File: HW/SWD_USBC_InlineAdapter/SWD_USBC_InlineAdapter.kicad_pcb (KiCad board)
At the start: 4 copper layers, 15.2 x 17.8 mm, 7 parts, among them J1 Conn_ARM_JTAG_SWD_10, J5 USB_C_Receptacle_USB2.0_14P, P1 USB_C_Plug

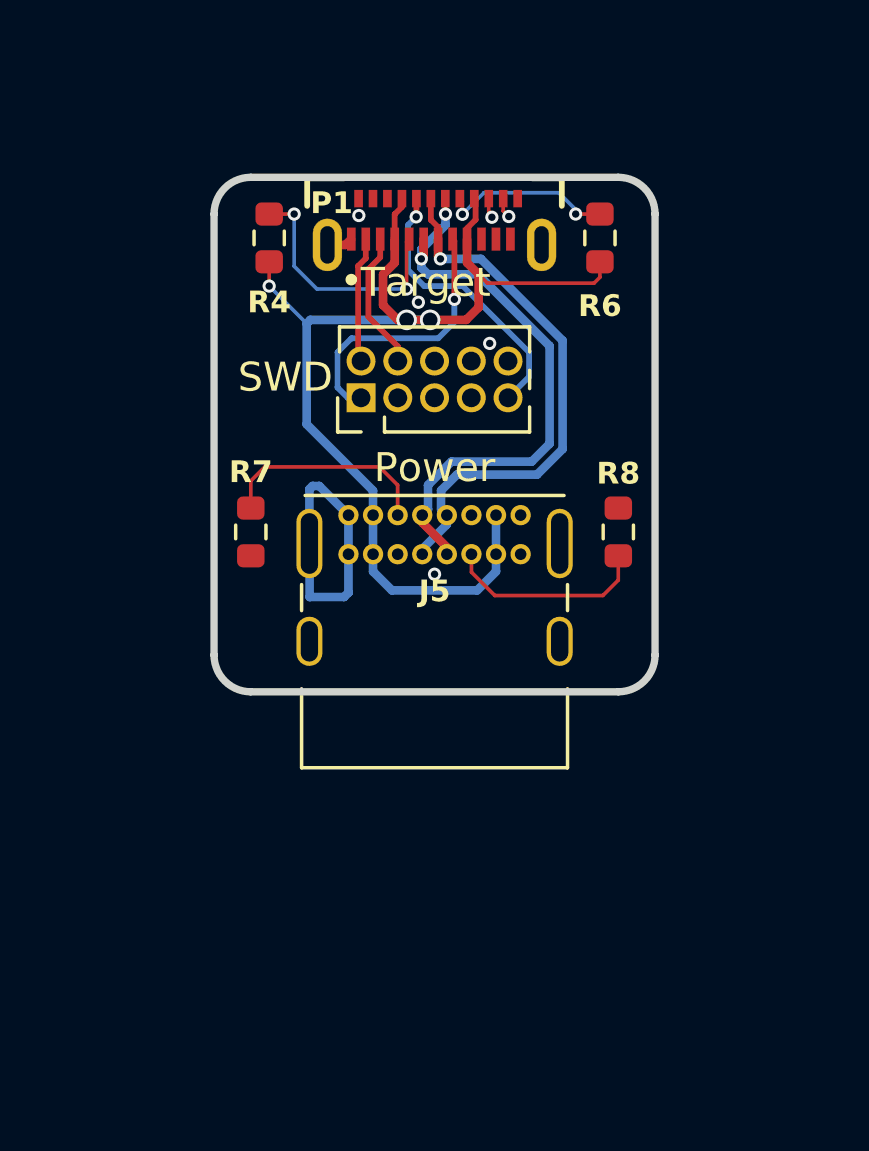
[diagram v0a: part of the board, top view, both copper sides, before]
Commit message: SWD to USB-C adapter 2026r2
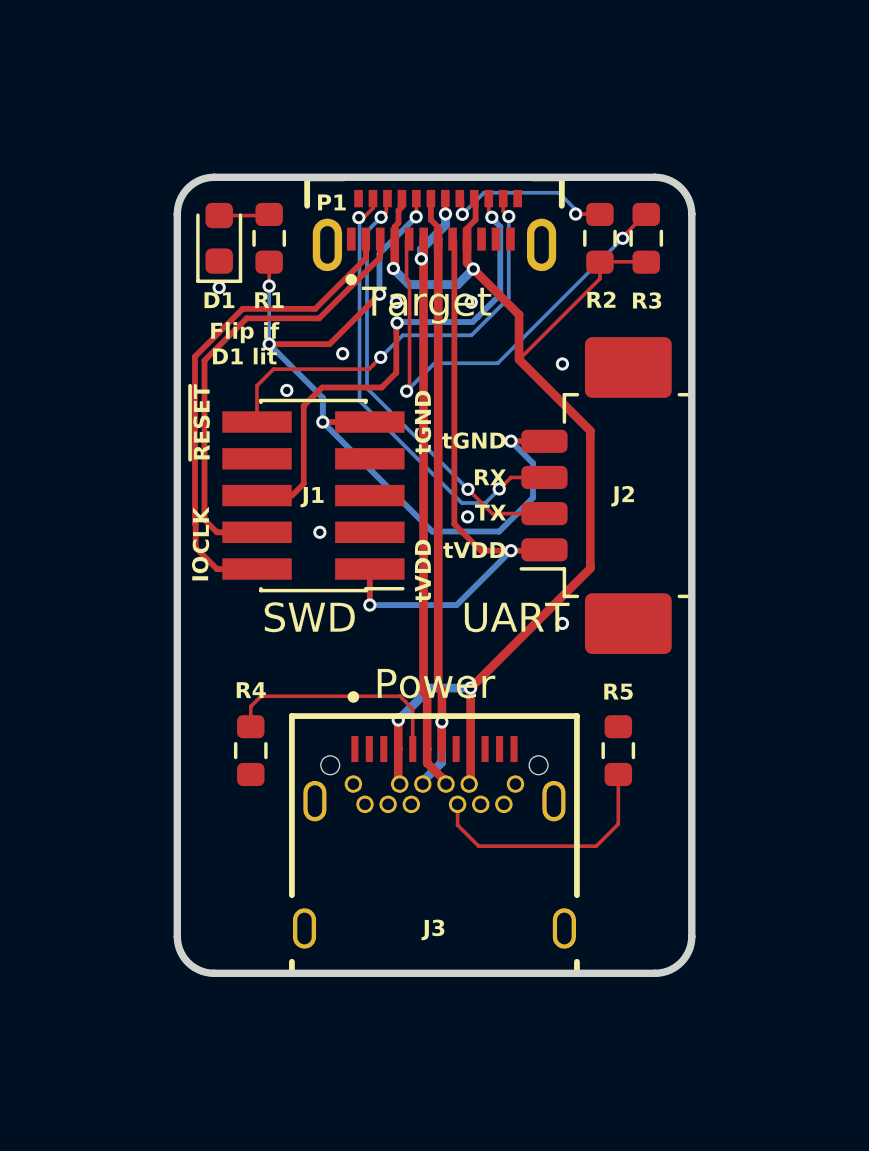
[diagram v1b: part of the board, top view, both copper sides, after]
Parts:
- removed J5: USB_C_Receptacle_USB2.0_14P, Connector_USB:USB_C_Receptacle_GCT_USB4085
- added D1: RED LED, Diode_SMD:D_0603_1608Metric, F.Cu at (52.2, 70.7)
- added J2: Conn_01x04, Connector_Molex:Molex_PicoBlade_53261-0471_1x04-1MP_P1.25mm_Horizontal, F.Cu at (65.9, 79.6)
- added J3: USB_C_Receptacle, USB4056_03_A:GCT_USB4056-03-A_REVA2, F.Cu at (59.7, 94.5)
- added R1: 100Ω, Resistor_SMD:R_0603_1608Metric, F.Cu at (54.0, 70.7)
- J1: footprint Connector_PinHeader_1.27mm:PinHeader_2x05_P1.27mm_Vertical -> Connector_PinHeader_1.27mm:PinHeader_2x05_P1.27mm_Vertical_SMD
- moved R3 13.0 mm to (67.0, 70.7)
- moved R4 7.56 mm to (53.3, 88.4)
- moved R5 7.56 mm to (66.0, 88.4)
- moved J1 3.76 mm to (55.5, 79.6), turned to 180 degrees
- renumbered R6 to R2, R4 to R3, R7 to R4, R8 to R5
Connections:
- net /Tgnd renamed /tGND
- net /VTref renamed /tVDD
- P1 pad B10: unconnected-(P1-RX1--PadB10) -> /UART_TXD
- P1 pad B11: unconnected-(P1-RX1+-PadB11) -> /UART_RXD
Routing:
- net /tGND: track 9.82 -> 29.0 mm, vias 1 -> 6
- net /UART_RXD: track 0.00 -> 15.5 mm, vias 0 -> 2
- net /UART_TXD: track 0.00 -> 14.8 mm, vias 0 -> 2
- net /SWDIO: track 4.37 -> 17.0 mm
- net /SWDCLK: track 4.80 -> 15.7 mm
- net /tVDD: track 9.54 -> 20.3 mm, vias 1 -> 2
- net GND: track 10.5 -> 0.04 mm, vias 4 -> 9
- net /SWO: track 7.13 -> 17.3 mm, vias 1 -> 2
- net /SWD~{RESET}: track 5.70 -> 14.7 mm, vias 1 -> 2
- net /CC1_T: track 8.64 -> 16.2 mm
- net /D-: track 18.8 -> 21.6 mm
- net Net-(D1-A): track 0.00 -> 1.74 mm
- net /D+: track 20.0 -> 21.7 mm
- net /CC2_SRC: track 7.09 -> 8.60 mm
- net +5V: track 39.9 -> 40.9 mm, vias 3 -> 4
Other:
- board size 15.2 x 17.8 mm -> 17.8 x 27.5 mm
- board text added: "${TITLE} Requests 5V @ 500mA Advertises 5V @ 500mA SWD: 2x05 1.27mm pitch UART: Molex PicoBlade 4-pin 1.25mm pitch Black Magic Probe pinout Daniel Stiner ${REVISION}"
- board text added: "CLK"
- board text added: "Flip if D1 lit"
- board text added: "IO"
- board text added: "Power"
- board text added: "RX"
- board text added: "SWD"
- board text added: "TX"
- board text added: "UART"
- board text added: "tGND"
- board text added: "tVDD"
- board text added: "~{RESET}"
- board text removed: "${TITLE} Supplies 5V @ 500mA Daniel Stiner ${REVISION}"
